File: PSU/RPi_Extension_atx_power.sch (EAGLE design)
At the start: 8 parts, among them J1 ATX24RH, J2 J2

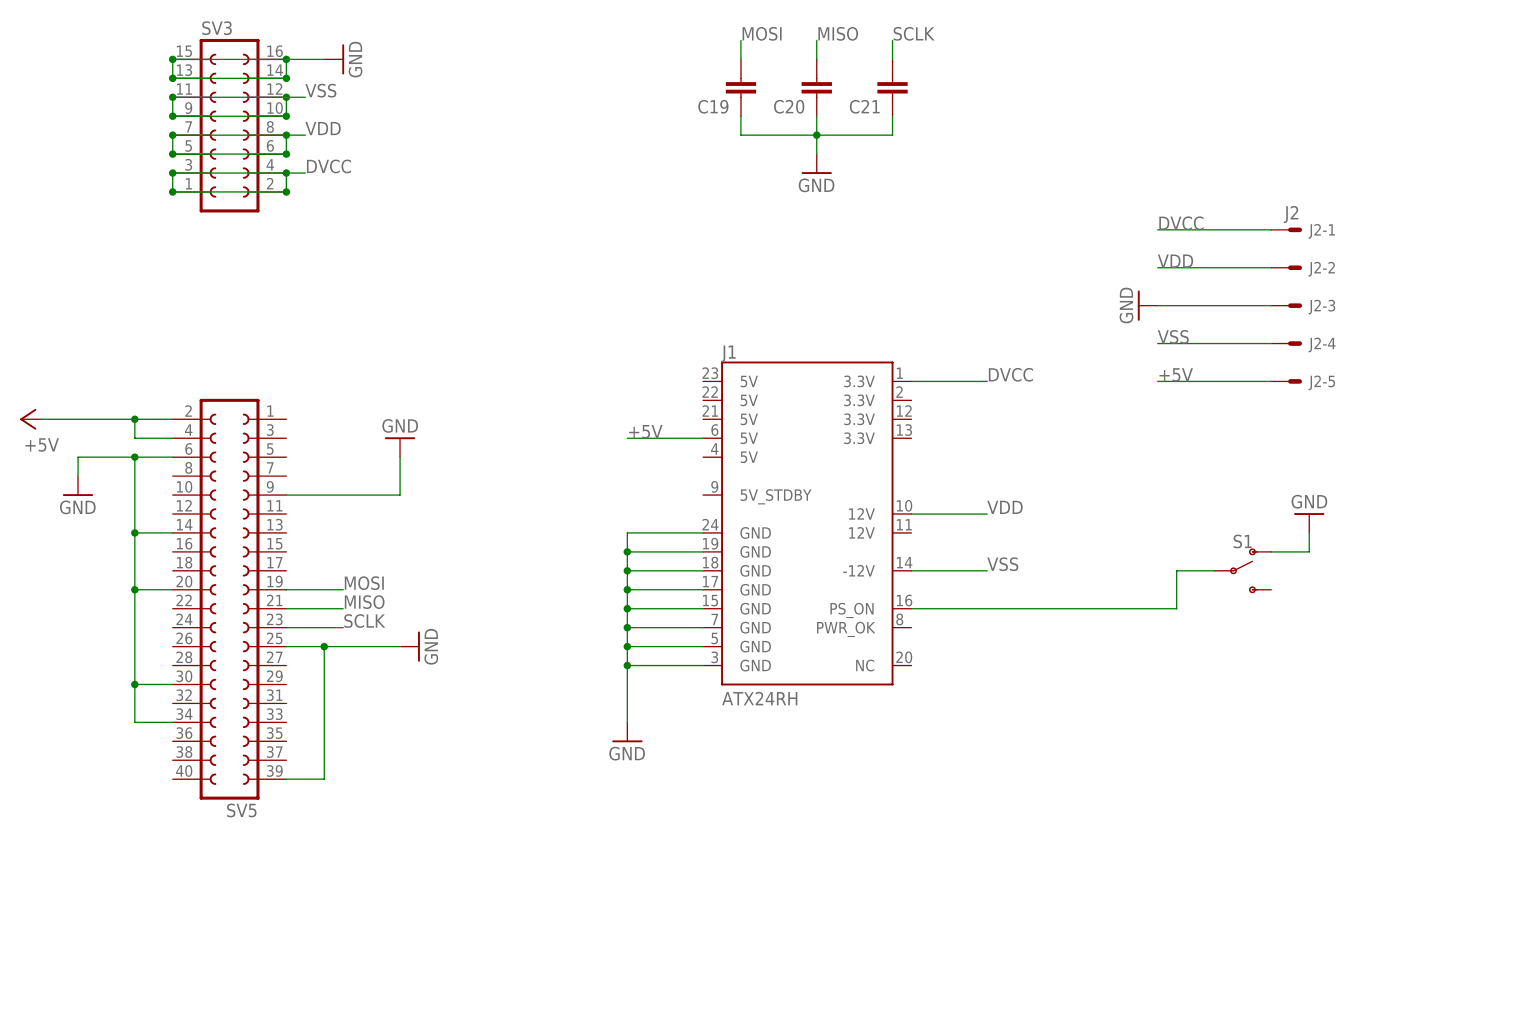
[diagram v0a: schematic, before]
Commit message: added vertical connector to power board
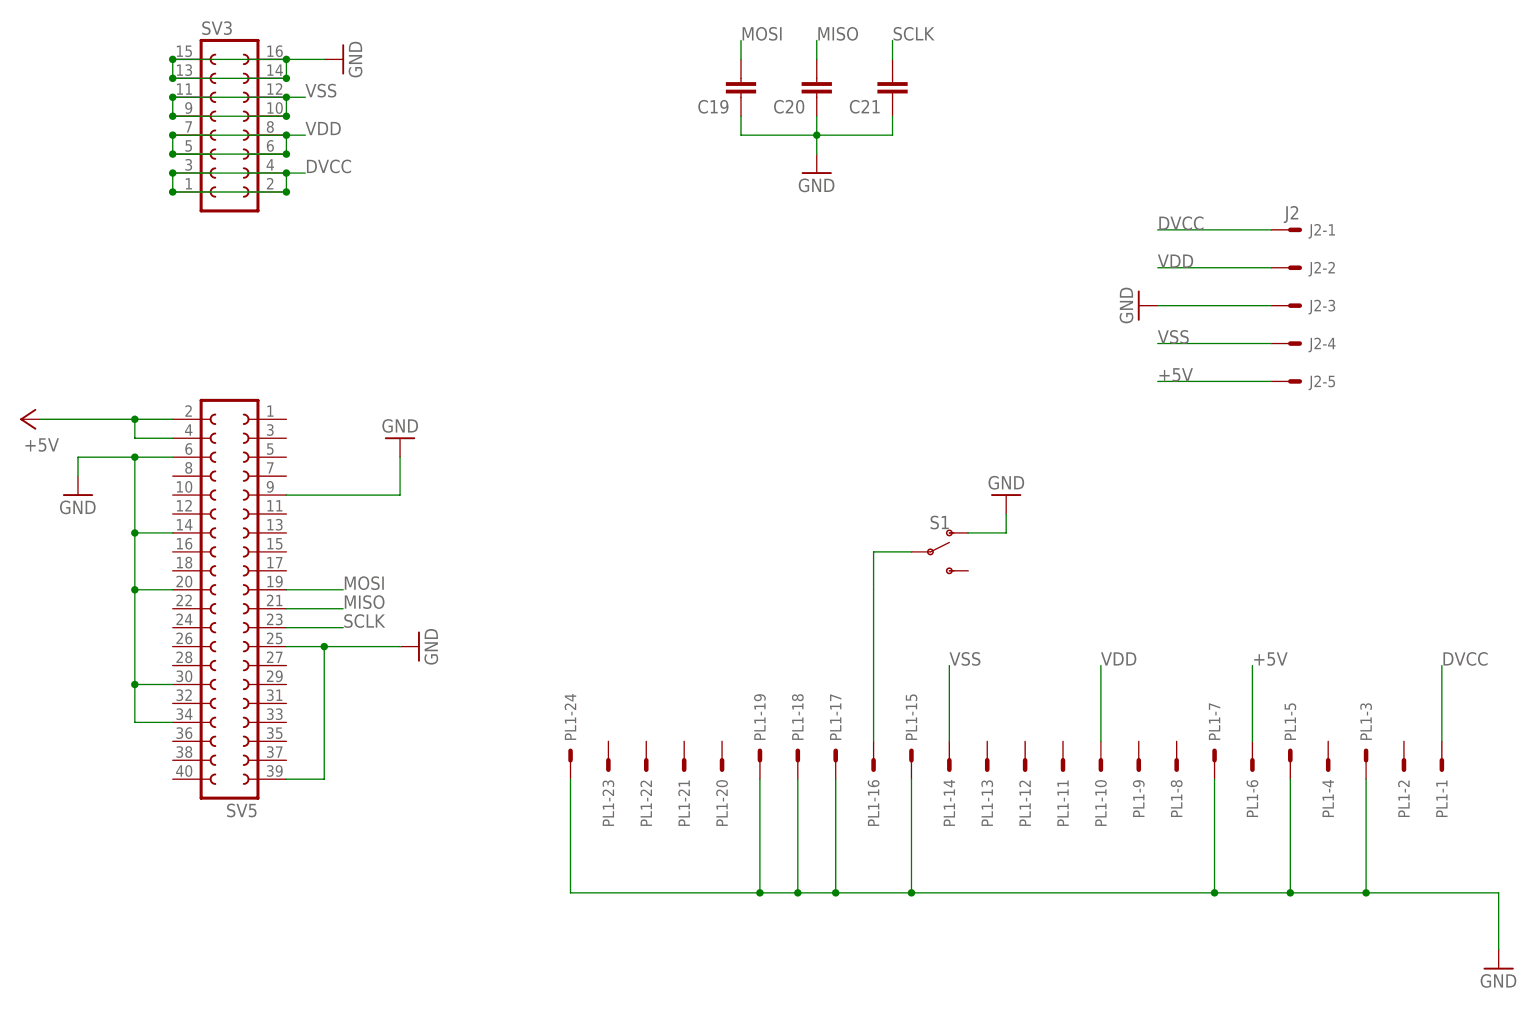
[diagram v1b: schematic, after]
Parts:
- removed J1: ATX24RH, SparkFun-Connectors:ATX24RH
- added PL1: (no value), con-molex-2:555X-24V
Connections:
- net +5V: now also PL1-6.S; no longer J1.5V@1
- net DVCC: now also PL1-1.S; no longer J1.3.3V@0
- net GND: now also PL1-15.S, PL1-17.S, PL1-18.S, PL1-19.S, PL1-24.S, PL1-3.S, PL1-5.S, PL1-7.S; no longer J1.GND@0, J1.GND@1, J1.GND@2, J1.GND@3, J1.GND@4, J1.GND@5, J1.GND@6, J1.GND@7
- net N$2: now also PL1-16.S; no longer J1.PS_ON
- net VDD: now also PL1-10.S; no longer J1.12V@0
- net VSS: now also PL1-14.S; no longer J1.-12V
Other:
- moved on the sheet: S1
